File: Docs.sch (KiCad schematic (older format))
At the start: 0 parts

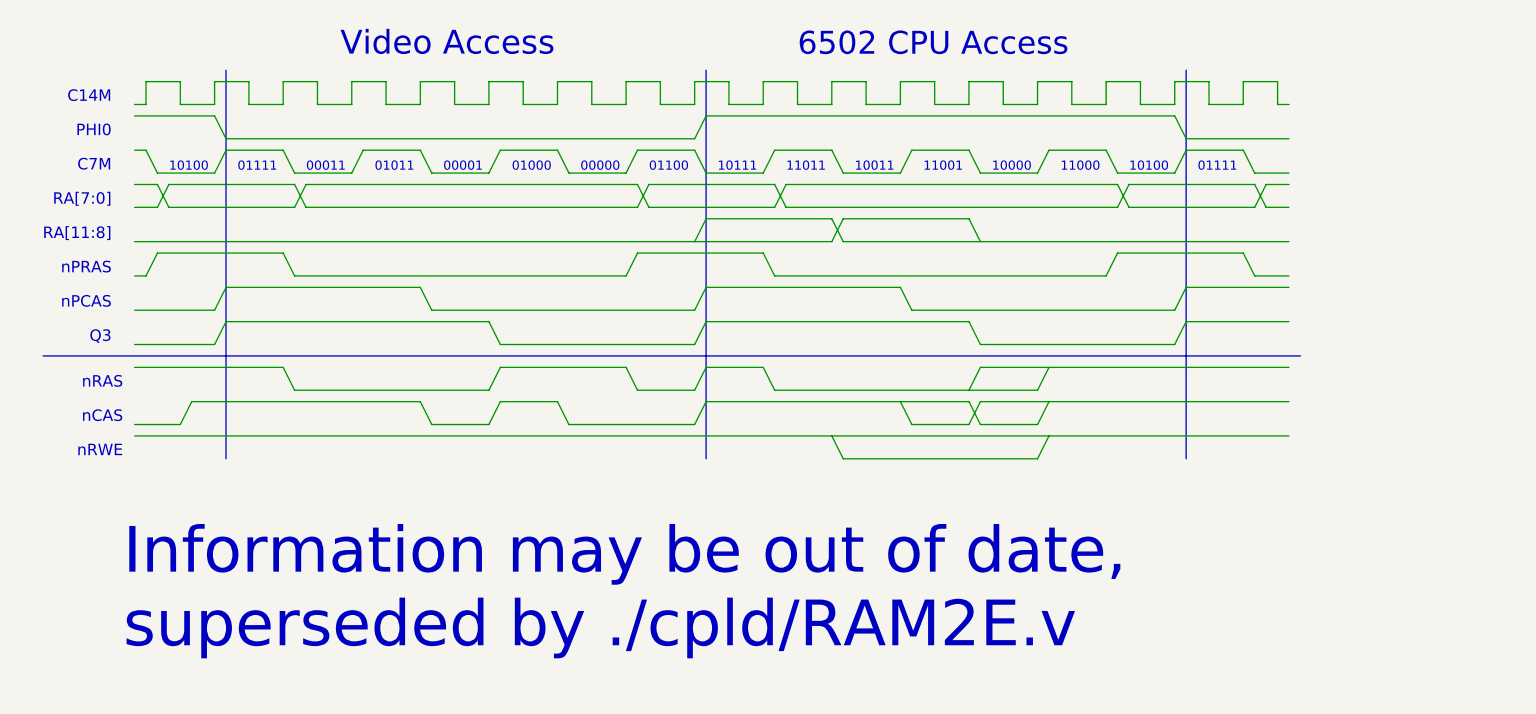
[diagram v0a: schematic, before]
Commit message: PLD: Delay EN80 like on Apple extended 80-column board
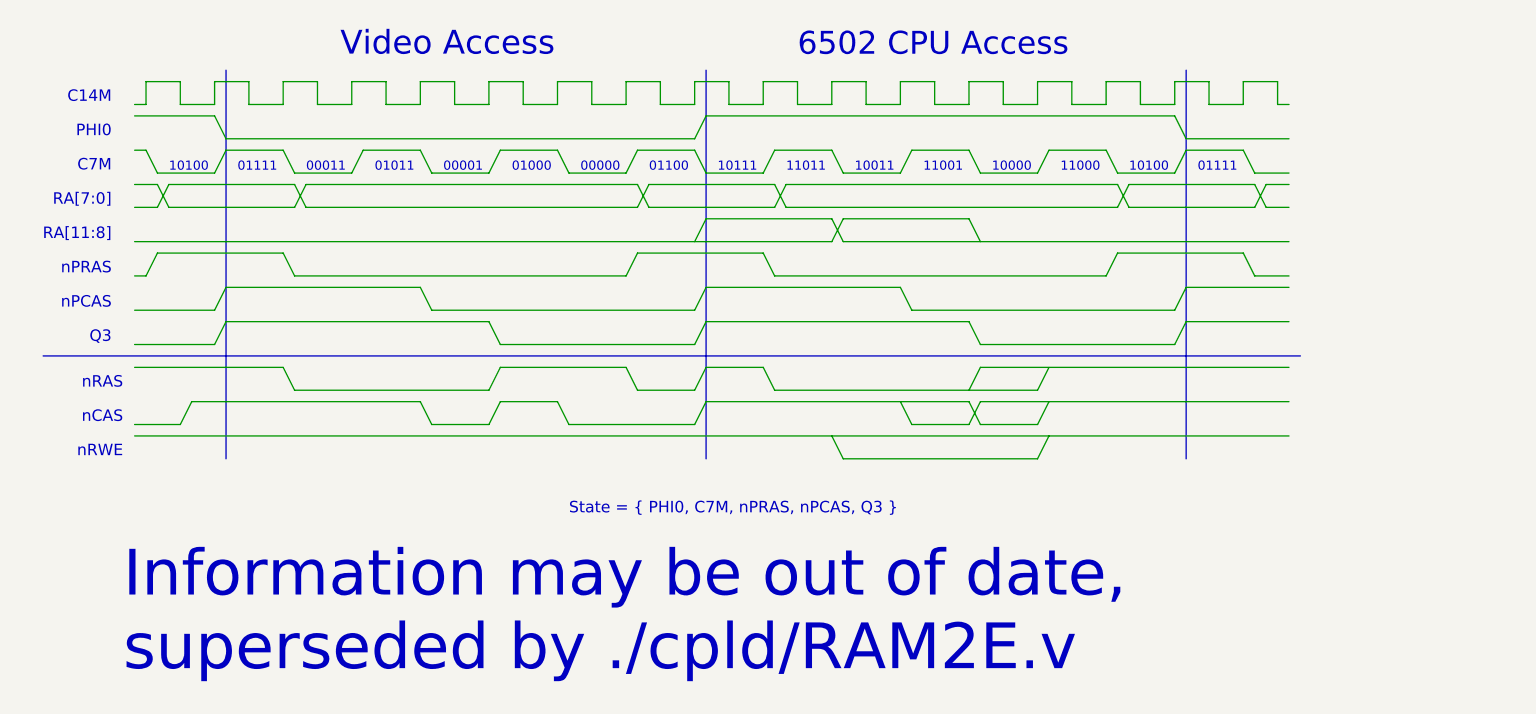
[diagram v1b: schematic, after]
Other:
- note added: "State = { PHI0, C7M, nPRAS, nPCAS, Q3 }"
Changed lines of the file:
@@
 Wire Wire Line
 	7500 1400 7500 1500
-Text Notes 3650 3900 0    200  ~ 0
+Text Notes 3650 4000 0    200  ~ 0
 Information may be out of date,\nsuperseded by ./cpld/RAM2E.v
 Wire Wire Line
@@
 Wire Wire Line
 	7350 2900 7400 2800
+Text Notes 5600 3300 0    50   ~ 0
+State = { PHI0, C7M, nPRAS, nPCAS, Q3 }
 $EndSCHEMATC

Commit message: Start redoing state...
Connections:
- wire segments 216 -> 208
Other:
- note removed: "nRWE"
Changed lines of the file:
@@
 EESchema Schematic File Version 4
 LIBS:RAM2E-cache
-EELAYER 29 0
+EELAYER 26 0
 EELAYER END
 $Descr A4 11693 8268
@@
 Text Notes 3650 2900 2    50   ~ 0
 nCAS
-Wire Bus Line
-	8300 1350 8300 3050
 Wire Wire Line
 	3950 2800 3900 2900
@@
 	8600 2250 8750 2250
 Wire Wire Line
-	6750 2950 6800 3050
-Wire Wire Line
 	6450 2150 6500 2250
 Wire Wire Line
@@
 	4050 2550 3700 2550
 Wire Bus Line
-	4100 1350 4100 3050
+	4100 1350 4100 2950
 Text Notes 3600 2100 2    50   ~ 0
 RA[11:8]
@@
 Wire Wire Line
 	7350 2000 7400 2100
-Text Notes 3650 3050 2    50   ~ 0
-nRWE
 Wire Wire Line
 	8250 1550 8300 1650
@@
 	6450 2650 6500 2750
 Wire Wire Line
-	7650 2900 7700 2800
+	8250 2900 8300 2800
 Wire Wire Line
 	7350 2800 7400 2900
@@
 	5000 2900 5250 2900
 Wire Bus Line
-	6200 1350 6200 3050
+	6200 1350 6200 2950
 Wire Wire Line
 	6550 1950 8000 1950
@@
 	3700 2100 6750 2100
 Wire Wire Line
-	7650 3050 7700 2950
-Wire Wire Line
 	5900 2750 6150 2750
 Wire Wire Line
@@
 	5600 2900 5550 2800
 Wire Wire Line
-	7350 2750 7400 2650
-Wire Wire Line
-	7400 2650 8750 2650
-Wire Wire Line
-	6800 3050 7650 3050
+	7700 2650 8750 2650
 Wire Wire Line
 	6200 1550 8250 1550
@@
 	7050 1500 7050 1400
 Wire Wire Line
-	3700 2950 8750 2950
-Wire Wire Line
 	6800 2000 7350 2000
 Wire Wire Line
 	6800 2100 8750 2100
 Wire Wire Line
-	7050 2800 7100 2900
-Wire Wire Line
-	7400 2900 7650 2900
-Wire Wire Line
 	6200 2800 7350 2800
-Wire Wire Line
-	7350 2900 7100 2900
-Wire Wire Line
-	7400 2800 8750 2800
-Wire Wire Line
-	7350 2900 7400 2800
 Text Notes 5600 3300 0    50   ~ 0
 State = { PHI0, C7M, nPRAS, nPCAS, Q3 }
+Wire Wire Line
+	8300 2800 8750 2800
+Wire Bus Line
+	8300 1350 8300 2950
+Wire Wire Line
+	7400 2900 8250 2900
 $EndSCHEMATC

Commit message: Changed to state counter
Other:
- note added: "0"
- note added: "1"
- note added: "2"
- note added: "3"
- note added: "4"
- note added: "5"
- note added: "6"
- note added: "7"
- note added: "8"
- note added: "9"
- note added: "A"
- note added: "B"
- note added: "C"
- note added: "D"
- note removed: "00000"
- note removed: "00001"
- note removed: "00011"
- note removed: "01000"
- note removed: "01011"
- note removed: "01100"
- note removed: "01111"
- note removed: "10000"
- note removed: "10011"
- note removed: "10111"
- note removed: "11000"
- note removed: "11001"
- note removed: "11011"
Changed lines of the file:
@@
 EESchema Schematic File Version 4
 LIBS:RAM2E-cache
-EELAYER 26 0
+EELAYER 29 0
 EELAYER END
 $Descr A4 11693 8268
@@
 Text Notes 6600 1300 0    100  ~ 0
 6502 CPU Access
-Text Notes 8350 1800 0    40   ~ 0
-01111
+Text Notes 8400 1800 0    40   ~ 0
+0
 Text Notes 3850 1800 0    40   ~ 0
 10100
@@
 Wire Wire Line
 	3750 1500 3700 1500
-Text Notes 8050 1800 0    40   ~ 0
-10100
-Text Notes 7750 1800 0    40   ~ 0
-11000
-Text Notes 7450 1800 0    40   ~ 0
-10000
+Text Notes 8100 1800 0    40   ~ 0
+D
+Text Notes 7800 1800 0    40   ~ 0
+C
+Text Notes 7500 1800 0    40   ~ 0
+B
 Wire Wire Line
 	5550 1700 5600 1800
@@
 Wire Wire Line
 	8600 1800 8750 1800
-Text Notes 5950 1800 0    40   ~ 0
-01100
-Text Notes 5650 1800 0    40   ~ 0
-00000
-Text Notes 5350 1800 0    40   ~ 0
-01000
-Text Notes 5050 1800 0    40   ~ 0
-00001
-Text Notes 4750 1800 0    40   ~ 0
-01011
-Text Notes 4450 1800 0    40   ~ 0
-00011
-Text Notes 4150 1800 0    40   ~ 0
-01111
-Text Notes 6250 1800 0    40   ~ 0
-10111
-Text Notes 6550 1800 0    40   ~ 0
-11011
+Text Notes 6000 1800 0    40   ~ 0
+6
+Text Notes 5700 1800 0    40   ~ 0
+5
+Text Notes 5400 1800 0    40   ~ 0
+4
+Text Notes 5100 1800 0    40   ~ 0
+3
+Text Notes 4800 1800 0    40   ~ 0
+2
+Text Notes 4200 1800 0    40   ~ 0
+0
+Text Notes 6300 1800 0    40   ~ 0
+7
+Text Notes 6600 1800 0    40   ~ 0
+8
 Wire Wire Line
 	8300 1650 8750 1650
@@
 Wire Wire Line
 	3800 1950 3700 1950
-Text Notes 6850 1800 0    40   ~ 0
-10011
-Text Notes 7150 1800 0    40   ~ 0
-11001
+Text Notes 6900 1800 0    40   ~ 0
+9
+Text Notes 7200 1800 0    40   ~ 0
+A
 Wire Wire Line
 	7500 1400 7500 1500
@@
 Wire Wire Line
 	7400 2900 8250 2900
+Text Notes 4500 1800 0    40   ~ 0
+1
 $EndSCHEMATC

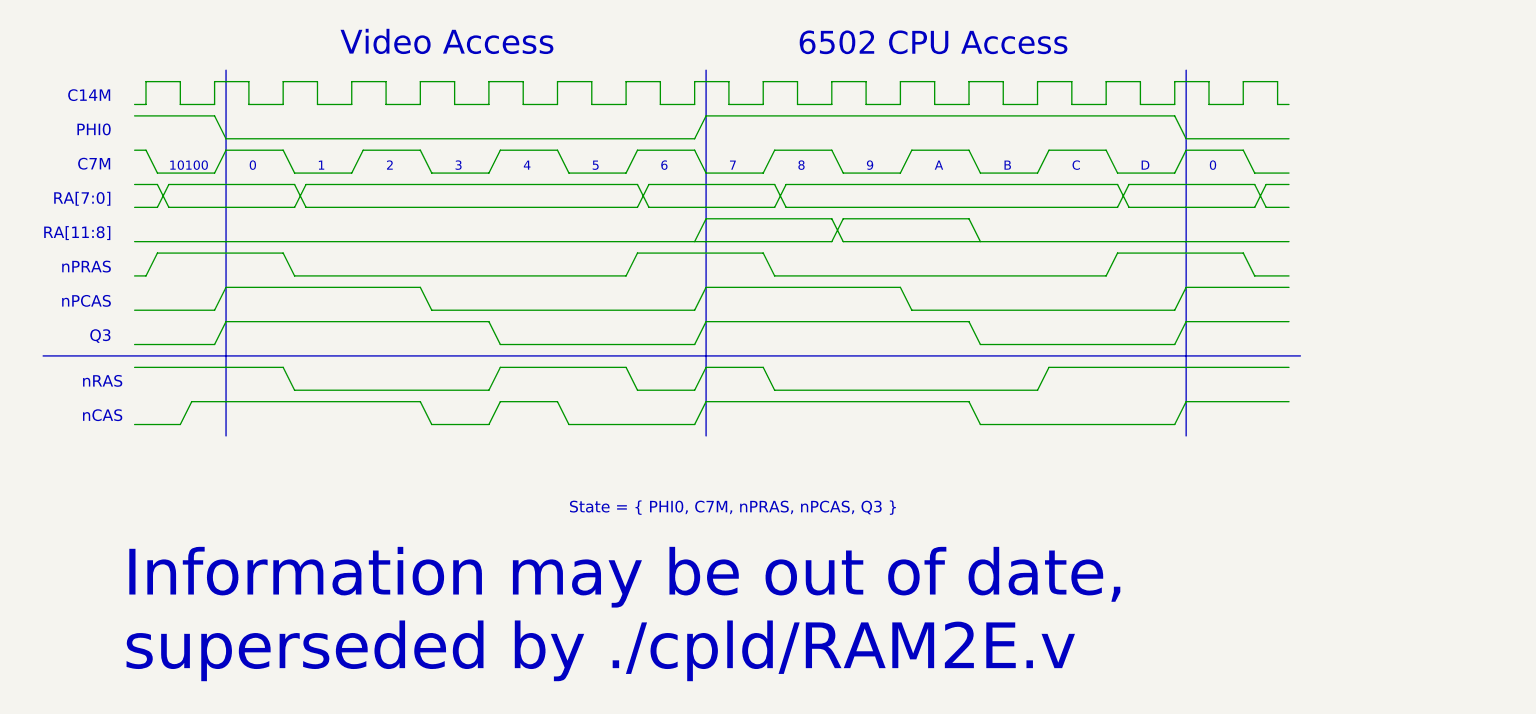
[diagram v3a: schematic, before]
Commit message: Timing fixes
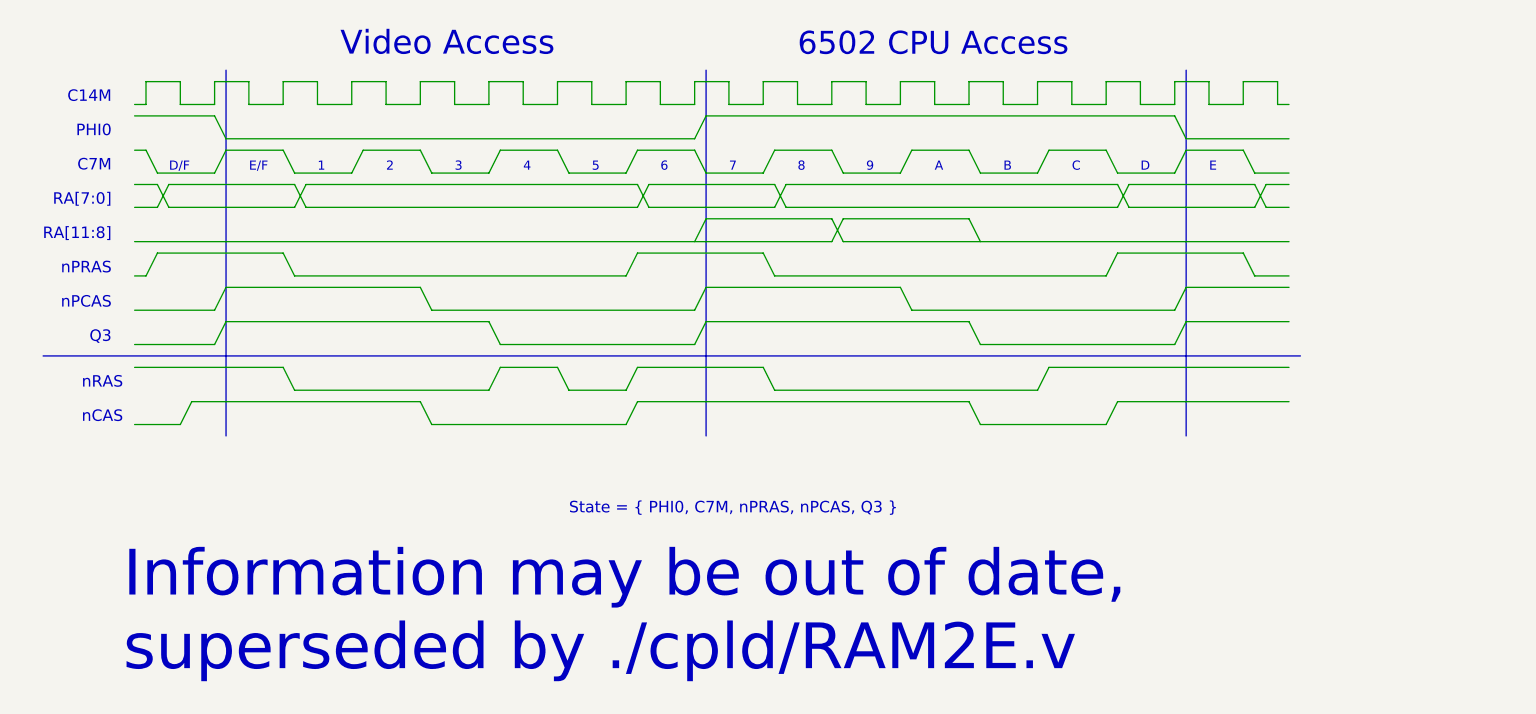
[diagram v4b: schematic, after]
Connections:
- wire segments 208 -> 204
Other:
- note added: "D/F"
- note added: "E"
- note added: "E/F"
- note removed: "0"
- note removed: "10100"
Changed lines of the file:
@@
 EESchema Schematic File Version 4
 LIBS:RAM2E-cache
-EELAYER 29 0
+EELAYER 26 0
 EELAYER END
 $Descr A4 11693 8268
@@
 6502 CPU Access
 Text Notes 8400 1800 0    40   ~ 0
-0
+E
 Text Notes 3850 1800 0    40   ~ 0
-10100
+D/F
 Wire Wire Line
 	3800 1800 4050 1800
@@
 2
 Text Notes 4200 1800 0    40   ~ 0
-0
+E/F
 Text Notes 6300 1800 0    40   ~ 0
 7
@@
 Wire Wire Line
 	5250 1500 5250 1400
-Wire Wire Line
-	5100 1500 5250 1500
 Wire Wire Line
 	4500 1500 4650 1500
@@
 	5250 2750 5300 2650
 Wire Wire Line
-	6450 2650 6200 2650
-Wire Wire Line
-	6200 2650 6150 2750
+	5900 2650 5850 2750
 Wire Wire Line
 	6450 2650 6500 2750
 Wire Wire Line
-	8250 2900 8300 2800
+	7950 2900 8000 2800
 Wire Wire Line
 	7350 2800 7400 2900
 Wire Wire Line
-	6200 2800 6150 2900
-Wire Wire Line
-	5250 2900 5300 2800
+	5900 2800 5850 2900
 Wire Wire Line
 	4950 2800 5000 2900
-Wire Wire Line
-	5000 2900 5250 2900
 Wire Bus Line
 	6200 1350 6200 2950
@@
 	3700 2100 6750 2100
 Wire Wire Line
-	5900 2750 6150 2750
-Wire Wire Line
-	5300 2650 5850 2650
-Wire Wire Line
-	5900 2750 5850 2650
-Wire Wire Line
-	5600 2900 6150 2900
-Wire Wire Line
-	5300 2800 5550 2800
-Wire Wire Line
-	5600 2900 5550 2800
+	5600 2750 5850 2750
+Wire Wire Line
+	5600 2750 5550 2650
 Wire Wire Line
 	7700 2650 8750 2650
@@
 Wire Wire Line
 	6800 2100 8750 2100
-Wire Wire Line
-	6200 2800 7350 2800
 Text Notes 5600 3300 0    50   ~ 0
 State = { PHI0, C7M, nPRAS, nPCAS, Q3 }
-Wire Wire Line
-	8300 2800 8750 2800
 Wire Bus Line
 	8300 1350 8300 2950
-Wire Wire Line
-	7400 2900 8250 2900
 Text Notes 4500 1800 0    40   ~ 0
 1
+Wire Wire Line
+	5900 2650 6450 2650
+Wire Wire Line
+	5000 2900 5850 2900
+Wire Wire Line
+	5300 2650 5550 2650
+Wire Wire Line
+	5900 2800 7350 2800
+Wire Wire Line
+	5100 1500 5250 1500
+Wire Wire Line
+	7400 2900 7950 2900
+Wire Wire Line
+	8000 2800 8750 2800
 $EndSCHEMATC
